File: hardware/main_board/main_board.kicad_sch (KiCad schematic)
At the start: 49 parts, among them J1 rgb 0, J10 uart, J11 input 4, J12 input 5, J13 rgb 3, J14 +5v out, J15 rgb 4, J16 input 6, J17 input 7, J18 rgb 5, J19 rgb output, J2 +12v 3a in, J20 ypbpr output, J21 rgb 6, J22 rgb 7, J3 input 0, J4 input 1, J5 icsp, J6 rgb 1, J7 input 2, J8 input 3, J9 rgb 2, SW10 prev, SW11 next, SW12 csync/rgbs, SW13 csync/rgbs, SW14 csync/rgbs, SW15 csync/rgbs, SW16 csync/rgbs, SW17 csync/rgbs, SW18 csync/rgbs, SW19 csync/rgbs, SW20 csync/rgbs, SW9 on/off, U1 ATmega328PB-A, U2 L7805

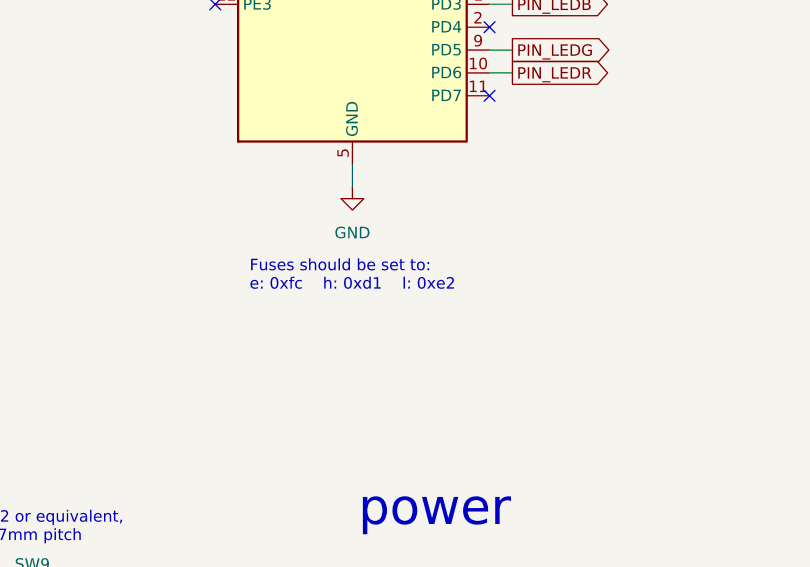
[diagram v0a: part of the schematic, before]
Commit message: #6: Update fuses to make sure boot reset vector is used.
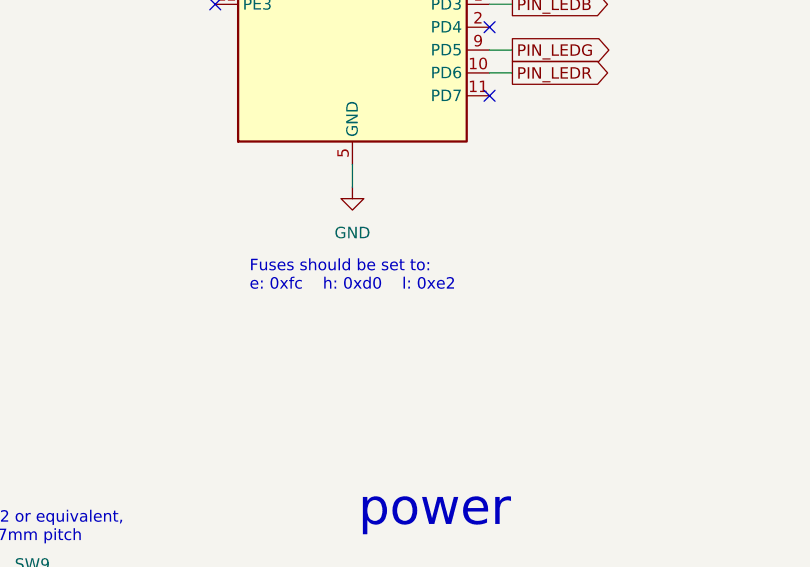
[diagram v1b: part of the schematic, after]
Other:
- note added: "Fuses should be set to: e: 0xfc h: 0xd0 l: 0xe2"
- note removed: "Fuses should be set to: e: 0xfc h: 0xd1 l: 0xe2"
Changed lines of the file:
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@@
 		)
 	)
-	(text "Fuses should be set to:\ne: 0xfc	h: 0xd1	l: 0xe2"
+	(text "Fuses should be set to:\ne: 0xfc	h: 0xd0	l: 0xe2"
 		(exclude_from_sim no)
 		(at 341.63 122.936 0)
